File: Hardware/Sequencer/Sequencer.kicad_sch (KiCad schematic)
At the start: 4 parts, among them J1 AudioJack2, SW2 SW_Omron_B3FS

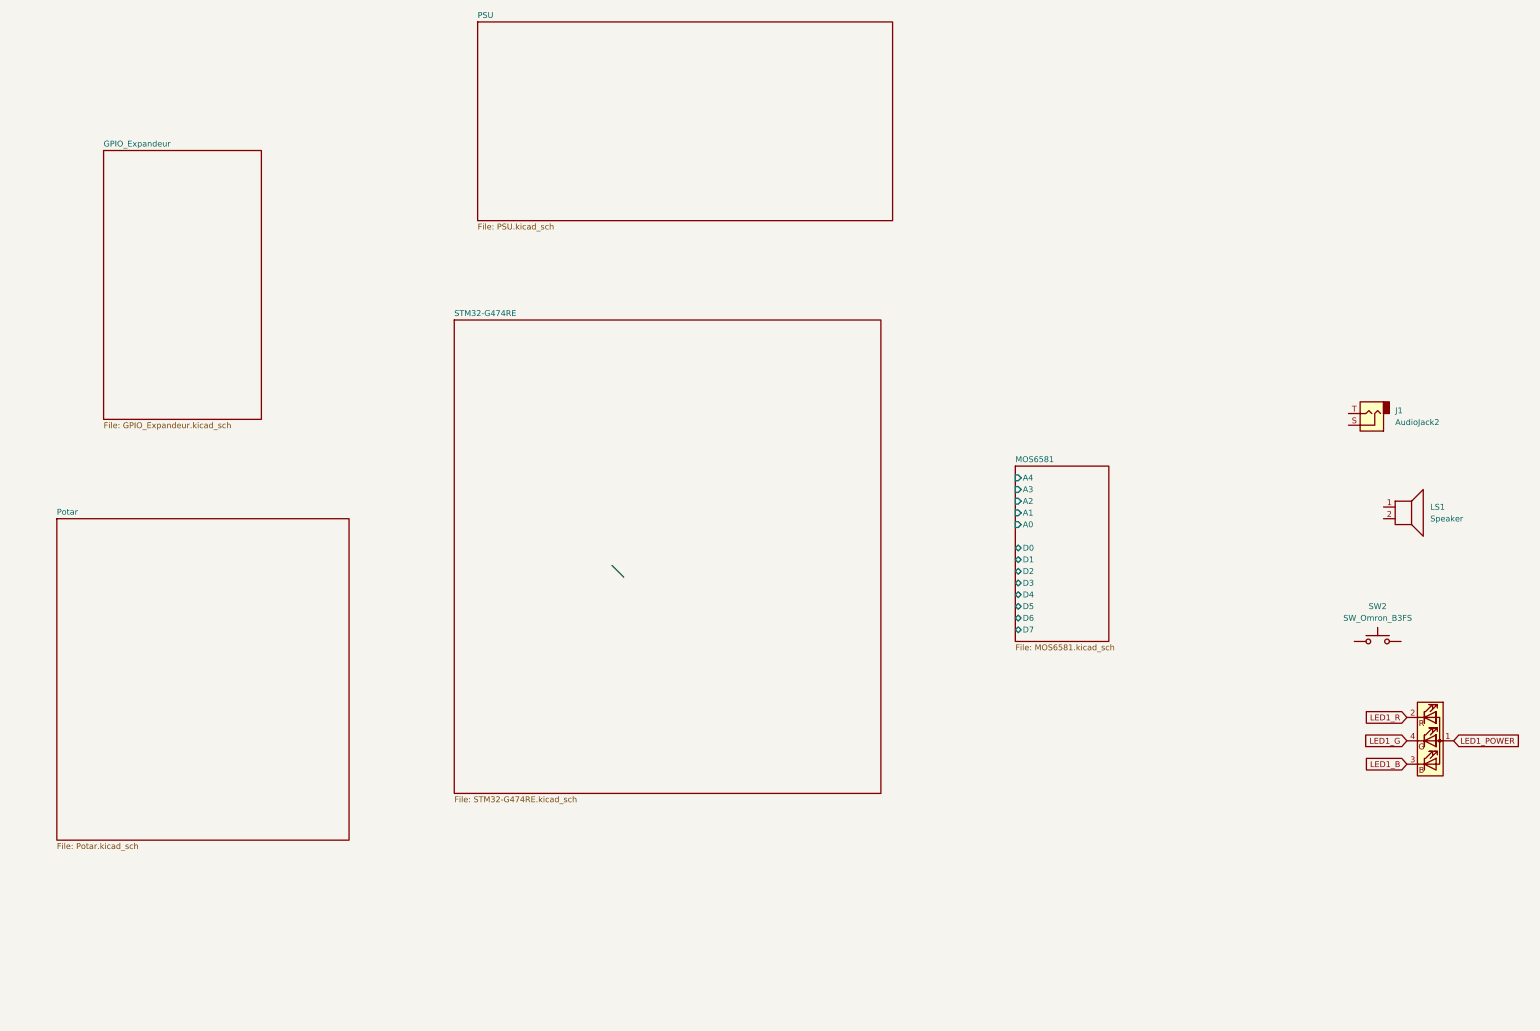
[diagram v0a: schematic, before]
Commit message: Beaucoup de changements sur le pcb
Alim corrigée, ajout de l'USB C

Sonde sur le processeur + linkage USB

Rajout des boutons (465M111...)
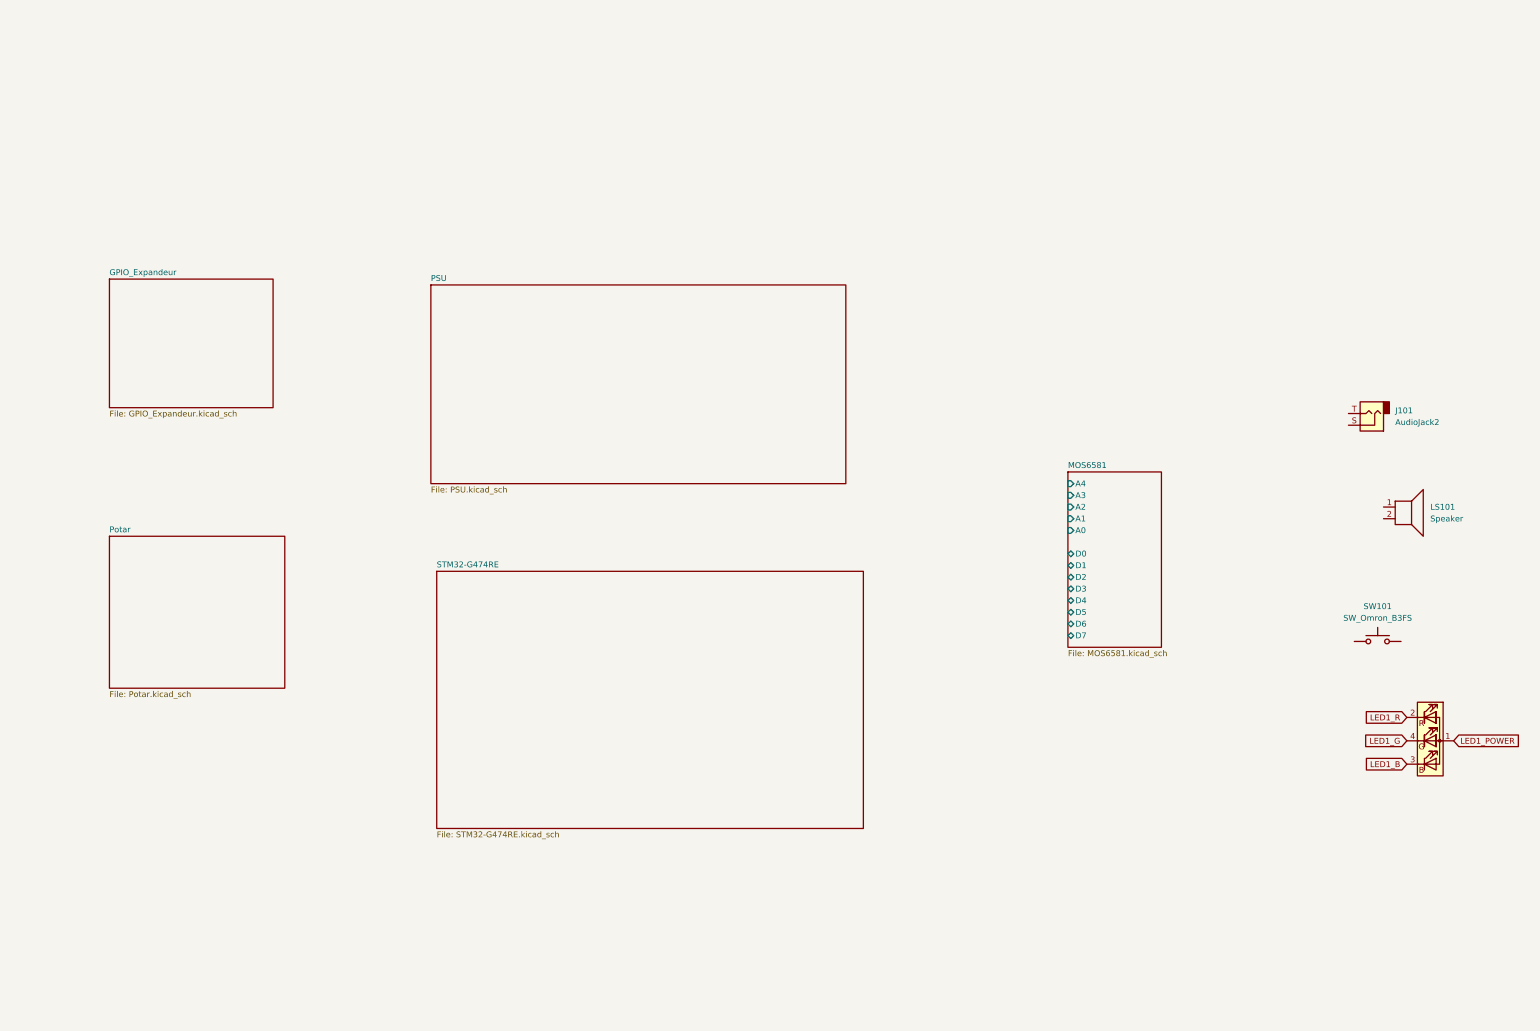
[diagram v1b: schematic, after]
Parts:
- renumbered D1 to D101, J1 to J101, LS1 to LS101, SW2 to SW101
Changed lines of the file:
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@@
 	(generator_version "8.0")
 	(paper "A4")
-	(bus_entry
-		(at 146.05 93.98)
-		(size 2.54 2.54)
-		(stroke
-			(width 0)
-			(type default)
-		)
-	)
 	(global_label "LED1_B"
 		(shape input)
@@
 		(dnp no)
 		(fields_autoplaced yes)
-		(property "Reference" "SW2"
+		(property "Reference" "SW101"
 			(at 312.42 102.87 0)
 			(effects
@@
 			(project "Sequencer"
 				(path "/bb3f736c-029c-4f1c-9c8c-1e3d4a336366"
-					(reference "SW2")
+					(reference "SW101")
 					(unit 1)
 				)
@@
 		(dnp no)
 		(fields_autoplaced yes)
-		(property "Reference" "LS1"
+		(property "Reference" "LS101"
 			(at 323.85 81.2799 0)
 			(effects
@@
 			(project "Sequencer"
 				(path "/bb3f736c-029c-4f1c-9c8c-1e3d4a336366"
-					(reference "LS1")
+					(reference "LS101")
 					(unit 1)
 				)
@@
 		(dnp no)
 		(fields_autoplaced yes)
-		(property "Reference" "J1"
+		(property "Reference" "J101"
 			(at 316.23 60.3249 0)
 			(effects
@@
 			(project "Sequencer"
 				(path "/bb3f736c-029c-4f1c-9c8c-1e3d4a336366"
-					(reference "J1")
+					(reference "J101")
 					(unit 1)
 				)
@@
 		(dnp no)
 		(fields_autoplaced yes)
-		(property "Reference" "D1"
+		(property "Reference" "D101"
 			(at 323.85 118.11 0)
 			(effects
@@
 			(project "Sequencer"
 				(path "/bb3f736c-029c-4f1c-9c8c-1e3d4a336366"
-					(reference "D1")
+					(reference "D101")
 					(unit 1)
 				)
@@
 	)
 	(sheet
-		(at 116.84 -24.13)
+		(at 106.68 33.02)
 		(size 90.17 43.18)
 		(fields_autoplaced yes)
@@
 		)
 		(property "Sheetname" "PSU"
-			(at 116.84 -24.8416 0)
+			(at 106.68 32.3084 0)
 			(effects
 				(font
@@
 		)
 		(property "Sheetfile" "PSU.kicad_sch"
-			(at 116.84 19.6346 0)
+			(at 106.68 76.7846 0)
 			(effects
 				(font
@@
 	)
 	(sheet
-		(at 25.4 83.82)
-		(size 63.5 69.85)
+		(at 36.83 87.63)
+		(size 38.1 33.02)
 		(fields_autoplaced yes)
 		(stroke
@@
 		)
 		(property "Sheetname" "Potar"
-			(at 25.4 83.1084 0)
+			(at 36.83 86.9184 0)
 			(effects
 				(font
@@
 		)
 		(property "Sheetfile" "Potar.kicad_sch"
-			(at 25.4 154.2546 0)
+			(at 36.83 121.2346 0)
 			(effects
 				(font
@@
 	)
 	(sheet
-		(at 233.68 72.39)
+		(at 245.11 73.66)
 		(size 20.32 38.1)
 		(fields_autoplaced yes)
@@
 		)
 		(property "Sheetname" "MOS6581"
-			(at 233.68 71.6784 0)
+			(at 245.11 72.9484 0)
 			(effects
 				(font
@@
 		)
 		(property "Sheetfile" "MOS6581.kicad_sch"
-			(at 233.68 111.0746 0)
+			(at 245.11 112.3446 0)
 			(effects
 				(font
@@
 		)
 		(pin "A4" input
-			(at 233.68 74.93 180)
+			(at 245.11 76.2 180)
 			(effects
 				(font
@@
 		)
 		(pin "A2" input
-			(at 233.68 80.01 180)
+			(at 245.11 81.28 180)
 			(effects
 				(font
@@
 		)
 		(pin "A0" input
-			(at 233.68 85.09 180)
+			(at 245.11 86.36 180)
 			(effects
 				(font
@@
 		)
 		(pin "A1" input
-			(at 233.68 82.55 180)
+			(at 245.11 83.82 180)
 			(effects
 				(font
@@
 		)
 		(pin "A3" input
-			(at 233.68 77.47 180)
+			(at 245.11 78.74 180)
 			(effects
 				(font
@@
 		)
 		(pin "D4" bidirectional
-			(at 233.68 100.33 180)
+			(at 245.11 101.6 180)
 			(effects
 				(font
@@
 		)
 		(pin "D2" bidirectional
-			(at 233.68 95.25 180)
+			(at 245.11 96.52 180)
 			(effects
 				(font
@@
 		)
 		(pin "D0" bidirectional
-			(at 233.68 90.17 180)
+			(at 245.11 91.44 180)
 			(effects
 				(font
@@
 		)
 		(pin "D1" bidirectional
-			(at 233.68 92.71 180)
+			(at 245.11 93.98 180)
 			(effects
 				(font
@@
 		)
 		(pin "D3" bidirectional
-			(at 233.68 97.79 180)
+			(at 245.11 99.06 180)
 			(effects
 				(font
@@
 		)
 		(pin "D6" bidirectional
-			(at 233.68 105.41 180)
+			(at 245.11 106.68 180)
 			(effects
 				(font
@@
 		)
 		(pin "D7" bidirectional
-			(at 233.68 107.95 180)
+			(at 245.11 109.22 180)
 			(effects
 				(font
@@
 		)
 		(pin "D5" bidirectional
-			(at 233.68 102.87 180)
+			(at 245.11 104.14 180)
 			(effects
 				(font
@@
 	)
 	(sheet
-		(at 35.56 3.81)
-		(size 34.29 58.42)
+		(at 36.83 31.75)
+		(size 35.56 27.94)
 		(fields_autoplaced yes)
 		(stroke
@@
 		)
 		(property "Sheetname" "GPIO_Expandeur"
-			(at 35.56 3.0984 0)
+			(at 36.83 31.0384 0)
 			(effects
 				(font
@@
 		)
 		(property "Sheetfile" "GPIO_Expandeur.kicad_sch"
-			(at 35.56 62.8146 0)
+			(at 36.83 60.2746 0)
 			(effects
 				(font
@@
 	)
 	(sheet
-		(at 111.76 40.64)
-		(size 92.71 102.87)
+		(at 107.95 95.25)
+		(size 92.71 55.88)
 		(fields_autoplaced yes)
 		(stroke
@@
 		)
 		(property "Sheetname" "STM32-G474RE"
-			(at 111.76 39.9284 0)
+			(at 107.95 94.5384 0)
 			(effects
 				(font
@@
 		)
 		(property "Sheetfile" "STM32-G474RE.kicad_sch"
-			(at 111.76 144.0946 0)
-			(effects
-				(font
+			(at 107.95 151.7146 0)
+			(effects
+				(font

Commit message: update dimension pcb, footprint
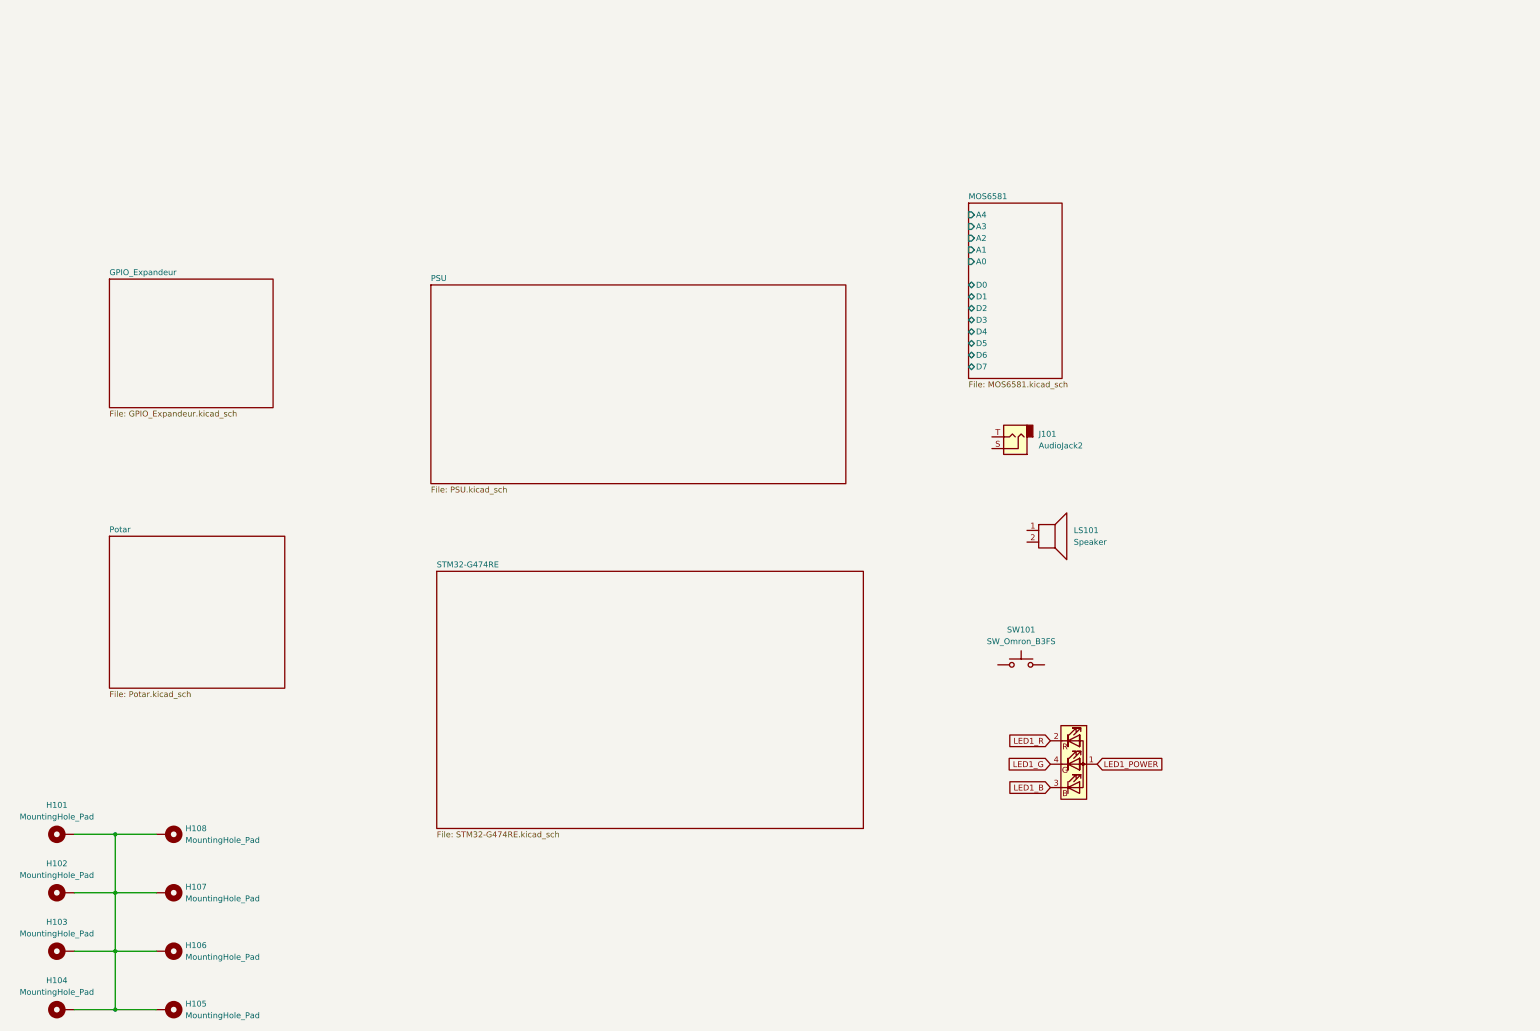
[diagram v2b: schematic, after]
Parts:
- added H101, H102, H103, H104, H105, H106, H107, H108: MountingHole_Pad, MountingHole:MountingHole_3.2mm_M3_Pad_Via, symbol Mechanical:MountingHole_Pad
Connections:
- new net: H101.1, H102.1, H103.1, H104.1, H105.1, H106.1, H107.1, H108.1
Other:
- moved on the sheet: J101, LS101, SW101

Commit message: much changes everywhere
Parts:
- removed D101: LED_ARBG, symbol Device:LED_ARBG
- removed SW101: SW_Omron_B3FS, symbol Switch:SW_Omron_B3FS
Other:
- sheet GPIO_Expandeur ports: added A0, A1, A2, A3, A4, A5, A6, A7, B0, B1, B10, B11, B12, B13, B14, B15, B2, B3, B4, B5, B6, B7, B8, B9, INTA_Boutons, INTB_Boutons, Reset, SCK Expandeur_Boutons, SCK LED_Driver, SDA Expandeur_Boutons, SDA LED_Driver; removed none
- sheet MOS6581 ports: added CLK_1MHZ, MOS6581_Read/Write, Reset; removed none
- sheet PSU ports: added USB_DM, USB_DP; removed none
- sheet Potar ports: added Filter_Freq_pot, Filter_Res_pot, Pitch_Main_pot, Pitch_octave_pot, Voice1_Attack_pot, Voice1_Decay_pot, Voice1_PW_pot, Voice1_Release_pot, Voice2_Attack_pot, Voice2_Decay_pot, Voice2_PW_pot, Voice2_Release_pot, Voice3_Attack_pot, Voice3_Decay_pot, Voice3_PW_pot, Voice3_Release_pot; removed none
- sheet STM32-G474RE ports: added ADC2_In10, USB_DM, USB_DP; removed none

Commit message: pcb
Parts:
- added C17: 100n, Capacitor_SMD:C_0402_1005Metric, symbol Device:C_Small
- added SW2: SW_Push_Dual_x2, symbol Switch:SW_Push_Dual_x2
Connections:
- new net: C17.1, SW2.1 (C)
- new net: C17.2, SW2.2 (D)
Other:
- sheet GPIO_Expandeur ports: added none; removed A0, A1, A2, A3, A4, A5, A6, A7, B0, B1, B10, B11, B12, B13, B14, B15, B2, B3, B4, B5, B6, B7, B8, B9
- sheet MOS6581 ports: added Audio_out; removed none
- sheet STM32-G474RE ports: added A0_SID, A1_SID, A2_SID, A3_SID, A4_SID, ADC1_In1, ADC1_In11, ADC1_In12, ADC1_In14, ADC1_In15, ADC1_In2, ADC1_In3, ADC1_In4, ADC1_In5, ADC1_In6, ADC1_In7, ADC1_In8, ADC1_In9, ADC2_In3, ADC2_In4, D0, D1, D2, D3, D4, D5, D6, D7, I2C_1_SCL, I2C_1_SDA, I2C_2_SCL, I2C_2_SDA, I2C_3_SCL, I2C_3_SDA; removed none
- note added: "Button TAP TEMPO !!FIND REF!! wurth"
- moved on the sheet: J101, LS101

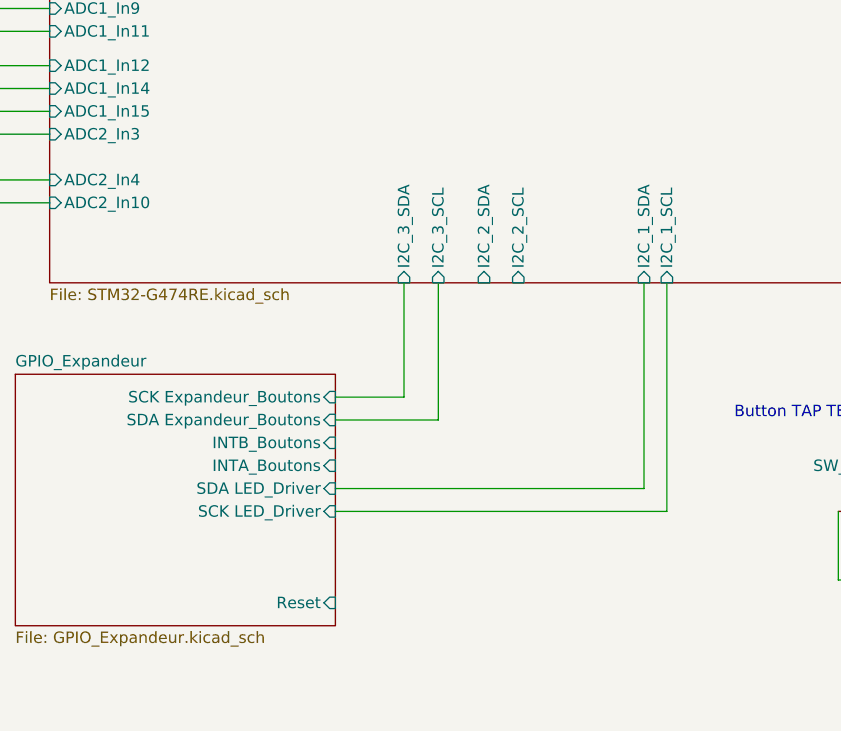
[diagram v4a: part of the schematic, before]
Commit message: SCHEMA CORRECTION LED
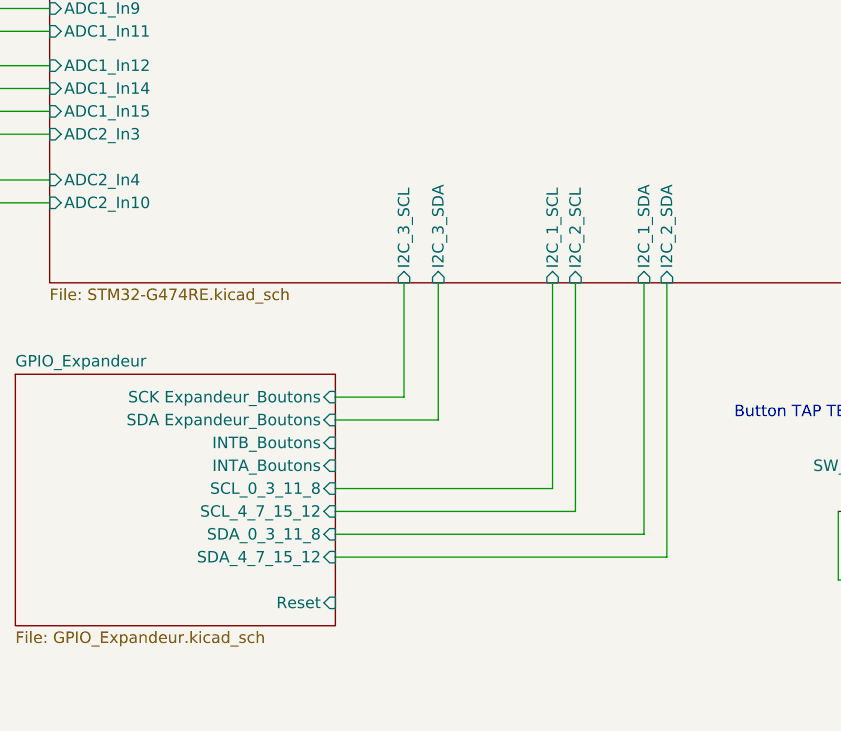
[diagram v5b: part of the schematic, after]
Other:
- sheet GPIO_Expandeur ports: added SCL_0_3_11_8, SCL_4_7_15_12, SDA_0_3_11_8, SDA_4_7_15_12; removed SCK LED_Driver, SDA LED_Driver

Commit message: update pcb
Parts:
- removed C17: 100n, Capacitor_SMD:C_0402_1005Metric, symbol Device:C_Small
- removed J101: AudioJack2, symbol Connector_Audio:AudioJack2
- removed LS101: Speaker, symbol Device:Speaker
- removed SW2: SW_Push_Dual_x2, symbol Switch:SW_Push_Dual_x2
- added C101: 10n, Capacitor_SMD:C_0402_1005Metric, symbol Device:C_Small
- added J101: LINEOUT, Connector_Audio:Jack_3.5mm_PJ320D_Horizontal, symbol Connector_Audio:AudioJack4
- added R101, R102: 10k, Resistor_SMD:R_0402_1005Metric, symbol Device:R_Small
- added SW101: SW_Push, Library:SMT Push Button 12x12, symbol Switch:SW_Push
- renumbered H108 to H105, H107 to H106, H106 to H107, H105 to H108
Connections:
- net MOS6581/Audio_out: now also J101.R1, J101.T
- new net +3.3V: R102.1
- new net GND: C101.2, J101.S, R101.2, R102.2, SW101.1, SW101.2
- new net STM32-G474RE/Tap_Tempo: C101.1, R101.1
- no-connect marks 0 -> 1
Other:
- sheet GPIO_Expandeur ports: added I2C_SCL, I2C_SDA, INTA_1, INTA_2, INTB_1, INTB_2; removed INTA_Boutons, INTB_Boutons, Reset, SCK Expandeur_Boutons, SCL_0_3_11_8, SCL_4_7_15_12, SDA Expandeur_Boutons, SDA_0_3_11_8, SDA_4_7_15_12
- sheet MOS6581 ports: added /Reset; removed Reset
- sheet STM32-G474RE ports: added INT1_A, INT1_B, INT2_A, INT2_B, MCO_1MHz, R/W_SID, Tap_Tempo, /RST_SID; removed I2C_1_SCL, I2C_1_SDA, I2C_2_SCL, I2C_2_SDA

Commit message: finalize pcb
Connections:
- net GND: now also H101.1, H102.1, H103.1, H104.1, H105.1, H106.1, H107.1, H108.1
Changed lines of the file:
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@@
+	)
+	(symbol
+		(lib_id "power:GND")
+		(at 38.1 152.4 180)
+		(unit 1)
+		(exclude_from_sim no)
+		(in_bom yes)
+		(on_board yes)
+		(dnp no)
+		(fields_autoplaced yes)
+		(property "Reference" "#PWR0104"
+			(at 38.1 146.05 0)
+			(effects
+				(font
+					(size 1.27 1.27)
+				)
+				(hide yes)
+			)
+		)
+		(property "Value" "GND"
+			(at 38.1 147.32 0)
+			(effects
+				(font
+					(size 1.27 1.27)
+				)
+			)
+		)
+		(property "Footprint" ""
+			(at 38.1 152.4 0)
+			(effects
+				(font
+					(size 1.27 1.27)
+				)
+				(hide yes)
+			)
+		)
+		(property "Datasheet" ""
+			(at 38.1 152.4 0)
+			(effects
+				(font
+					(size 1.27 1.27)
+				)
+				(hide yes)
+			)
+		)
+		(property "Description" "Power symbol creates a global label with name \"GND\" , ground"
+			(at 38.1 152.4 0)
+			(effects
+				(font
+					(size 1.27 1.27)
+				)
+				(hide yes)
+			)
+		)
+		(pin "1"
+		)
+		(instances
+			(project "Sequencer"
+				(path "/bb3f736c-029c-4f1c-9c8c-1e3d4a336366"
+					(reference "#PWR0104")
+					(unit 1)
+				)
+			)
+		)
 	)
 	(symbol
